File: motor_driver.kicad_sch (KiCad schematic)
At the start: 8 parts, among them J4 Conn_01x06, J5 Conn_01x06, U11 TB6612FNG

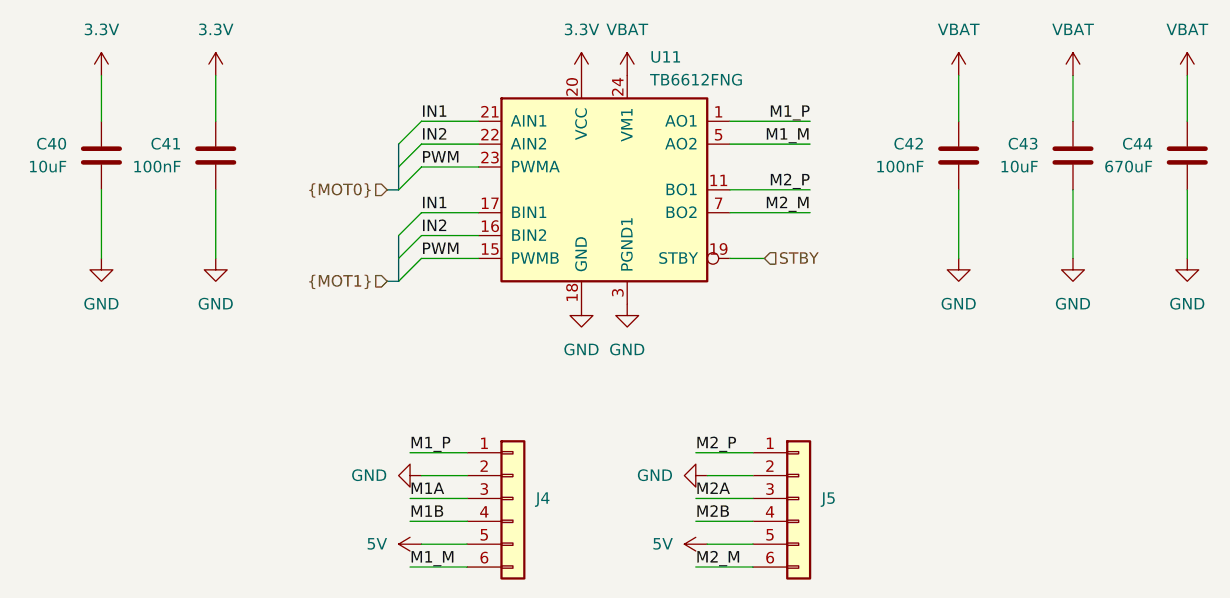
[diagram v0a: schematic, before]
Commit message: Add missing pull-up for CP2102
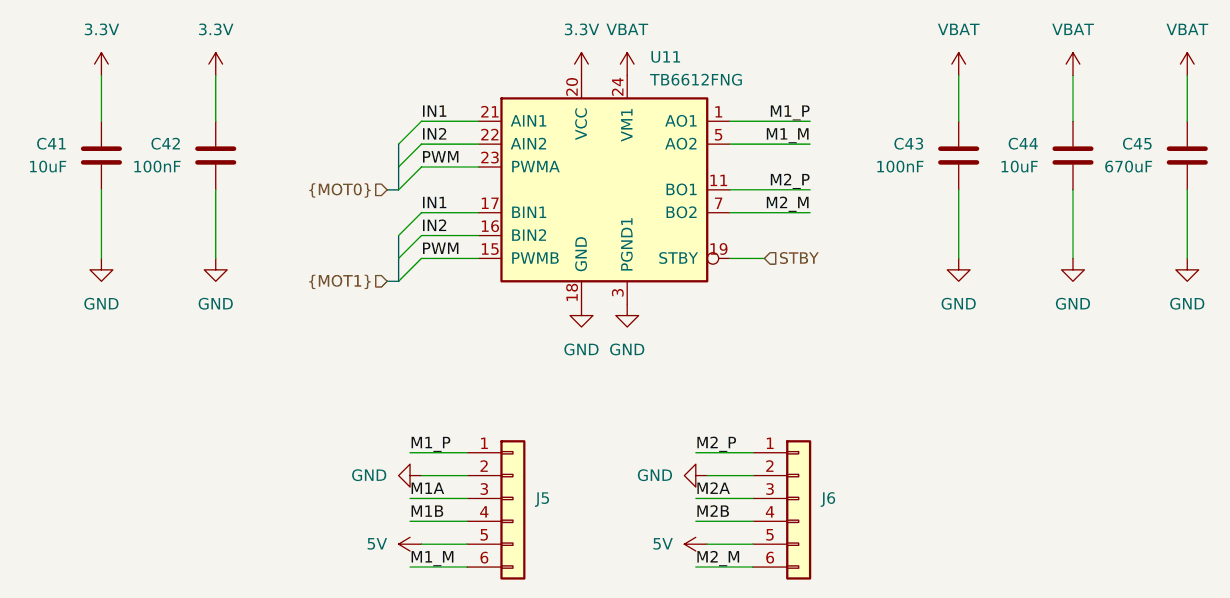
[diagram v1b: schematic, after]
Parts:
- renumbered C40 to C41, C41 to C42, C42 to C43, C43 to C44, C44 to C45, J4 to J5, J5 to J6
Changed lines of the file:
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@@
 		(dnp no)
 		(fields_autoplaced yes)
-		(property "Reference" "#PWR0134"
+		(property "Reference" "#PWR0140"
 			(at 212.09 78.74 0)
 			(effects
@@
 			(project "Tumbler2_Redesign"
 				(path "/f3fd8d79-9d35-4c04-811e-2697a2740958/f393b342-ddad-47d4-8b4e-f21b64e15add"
-					(reference "#PWR0134")
+					(reference "#PWR0140")
 					(unit 1)
 				)
@@
 		(dnp no)
 		(fields_autoplaced yes)
-		(property "Reference" "#PWR0143"
+		(property "Reference" "#PWR0149"
 			(at 152.4 119.38 0)
 			(effects
@@
 			(project "Tumbler2_Redesign"
 				(path "/f3fd8d79-9d35-4c04-811e-2697a2740958/f393b342-ddad-47d4-8b4e-f21b64e15add"
-					(reference "#PWR0143")
+					(reference "#PWR0149")
 					(unit 1)
 				)
@@
 		(dnp no)
 		(fields_autoplaced yes)
-		(property "Reference" "#PWR0129"
+		(property "Reference" "#PWR0137"
 			(at 149.86 78.74 0)
 			(effects
@@
 			(project "Tumbler2_Redesign"
 				(path "/f3fd8d79-9d35-4c04-811e-2697a2740958/f393b342-ddad-47d4-8b4e-f21b64e15add"
-					(reference "#PWR0129")
+					(reference "#PWR0137")
 					(unit 1)
 				)
@@
 		(dnp no)
 		(fields_autoplaced yes)
-		(property "Reference" "#PWR0128"
+		(property "Reference" "#PWR0136"
 			(at 144.78 78.74 0)
 			(effects
@@
 			(project "Tumbler2_Redesign"
 				(path "/f3fd8d79-9d35-4c04-811e-2697a2740958/f393b342-ddad-47d4-8b4e-f21b64e15add"
-					(reference "#PWR0128")
+					(reference "#PWR0136")
 					(unit 1)
 				)
@@
 		(dnp no)
 		(fields_autoplaced yes)
-		(property "Reference" "#PWR0144"
+		(property "Reference" "#PWR0150"
 			(at 130.81 127 0)
 			(effects
@@
 			(project "Tumbler2_Redesign"
 				(path "/f3fd8d79-9d35-4c04-811e-2697a2740958/f393b342-ddad-47d4-8b4e-f21b64e15add"
-					(reference "#PWR0144")
+					(reference "#PWR0150")
 					(unit 1)
 				)
@@
 		(on_board yes)
 		(dnp no)
-		(property "Reference" "C41"
+		(property "Reference" "C42"
 			(at 100.33 82.5499 0)
 			(effects
@@
 			(project "Tumbler2_Redesign"
 				(path "/f3fd8d79-9d35-4c04-811e-2697a2740958/f393b342-ddad-47d4-8b4e-f21b64e15add"
-					(reference "C41")
+					(reference "C42")
 					(unit 1)
 				)
@@
 		(dnp no)
 		(fields_autoplaced yes)
-		(property "Reference" "#PWR0145"
+		(property "Reference" "#PWR0151"
 			(at 162.56 127 0)
 			(effects
@@
 			(project "Tumbler2_Redesign"
 				(path "/f3fd8d79-9d35-4c04-811e-2697a2740958/f393b342-ddad-47d4-8b4e-f21b64e15add"
-					(reference "#PWR0145")
+					(reference "#PWR0151")
 					(unit 1)
 				)
@@
 		(on_board yes)
 		(dnp no)
-		(property "Reference" "C43"
+		(property "Reference" "C44"
 			(at 195.58 82.5499 0)
 			(effects
@@
 			(project "Tumbler2_Redesign"
 				(path "/f3fd8d79-9d35-4c04-811e-2697a2740958/f393b342-ddad-47d4-8b4e-f21b64e15add"
-					(reference "C43")
+					(reference "C44")
 					(unit 1)
 				)
@@
 		(dnp no)
 		(fields_autoplaced yes)
-		(property "Reference" "#PWR0136"
+		(property "Reference" "#PWR0142"
 			(at 104.14 101.6 0)
 			(effects
@@
 			(project "Tumbler2_Redesign"
 				(path "/f3fd8d79-9d35-4c04-811e-2697a2740958/f393b342-ddad-47d4-8b4e-f21b64e15add"
-					(reference "#PWR0136")
+					(reference "#PWR0142")
 					(unit 1)
 				)
@@
 		(dnp no)
 		(fields_autoplaced yes)
-		(property "Reference" "#PWR0137"
+		(property "Reference" "#PWR0146"
 			(at 144.78 106.68 0)
 			(effects
@@
 			(project "Tumbler2_Redesign"
 				(path "/f3fd8d79-9d35-4c04-811e-2697a2740958/f393b342-ddad-47d4-8b4e-f21b64e15add"
-					(reference "#PWR0137")
+					(reference "#PWR0146")
 					(unit 1)
 				)
@@
 		(dnp no)
 		(fields_autoplaced yes)
-		(property "Reference" "#PWR0142"
+		(property "Reference" "#PWR0148"
 			(at 120.65 119.38 0)
 			(effects
@@
 			(project "Tumbler2_Redesign"
 				(path "/f3fd8d79-9d35-4c04-811e-2697a2740958/f393b342-ddad-47d4-8b4e-f21b64e15add"
-					(reference "#PWR0142")
+					(reference "#PWR0148")
 					(unit 1)
 				)
@@
 		(dnp no)
 		(fields_autoplaced yes)
-		(property "Reference" "#PWR0132"
+		(property "Reference" "#PWR0138"
 			(at 186.69 78.74 0)
 			(effects
@@
 			(project "Tumbler2_Redesign"
 				(path "/f3fd8d79-9d35-4c04-811e-2697a2740958/f393b342-ddad-47d4-8b4e-f21b64e15add"
-					(reference "#PWR0132")
+					(reference "#PWR0138")
 					(unit 1)
 				)
@@
 		(dnp no)
 		(fields_autoplaced yes)
-		(property "Reference" "#PWR0141"
+		(property "Reference" "#PWR0145"
 			(at 212.09 101.6 0)
 			(effects
@@
 			(project "Tumbler2_Redesign"
 				(path "/f3fd8d79-9d35-4c04-811e-2697a2740958/f393b342-ddad-47d4-8b4e-f21b64e15add"
-					(reference "#PWR0141")
+					(reference "#PWR0145")
 					(unit 1)
 				)
@@
 		(on_board yes)
 		(dnp no)
-		(property "Reference" "C44"
+		(property "Reference" "C45"
 			(at 208.28 82.5499 0)
 			(effects
@@
 			(project "Tumbler2_Redesign"
 				(path "/f3fd8d79-9d35-4c04-811e-2697a2740958/f393b342-ddad-47d4-8b4e-f21b64e15add"
-					(reference "C44")
+					(reference "C45")
 					(unit 1)
 				)
@@
 		(dnp no)
 		(fields_autoplaced yes)
-		(property "Reference" "#PWR0140"
+		(property "Reference" "#PWR0144"
 			(at 199.39 101.6 0)
 			(effects
@@
 			(project "Tumbler2_Redesign"
 				(path "/f3fd8d79-9d35-4c04-811e-2697a2740958/f393b342-ddad-47d4-8b4e-f21b64e15add"
-					(reference "#PWR0140")
+					(reference "#PWR0144")
 					(unit 1)
 				)
@@
 		(dnp no)
 		(fields_autoplaced yes)
-		(property "Reference" "#PWR0131"
+		(property "Reference" "#PWR0135"
 			(at 104.14 78.74 0)
 			(effects
@@
 			(project "Tumbler2_Redesign"
 				(path "/f3fd8d79-9d35-4c04-811e-2697a2740958/f393b342-ddad-47d4-8b4e-f21b64e15add"
-					(reference "#PWR0131")
+					(reference "#PWR0135")
 					(unit 1)
 				)
@@
 		(on_board yes)
 		(dnp no)
-		(property "Reference" "J5"
+		(property "Reference" "J6"
 			(at 171.45 121.9199 0)
 			(effects
@@
 			(project "Tumbler2_Redesign"
 				(path "/f3fd8d79-9d35-4c04-811e-2697a2740958/f393b342-ddad-47d4-8b4e-f21b64e15add"
-					(reference "J5")
+					(reference "J6")
 					(unit 1)
 				)
@@
 		(dnp no)
 		(fields_autoplaced yes)
-		(property "Reference" "#PWR0139"
+		(property "Reference" "#PWR0143"
 			(at 186.69 101.6 0)
 			(effects
@@
 			(project "Tumbler2_Redesign"
 				(path "/f3fd8d79-9d35-4c04-811e-2697a2740958/f393b342-ddad-47d4-8b4e-f21b64e15add"
-					(reference "#PWR0139")
+					(reference "#PWR0143")
 					(unit 1)
 				)
@@
 		(on_board yes)
 		(dnp no)
-		(property "Reference" "J4"
+		(property "Reference" "J5"
 			(at 139.7 121.9199 0)
 			(effects
@@
 			(project "Tumbler2_Redesign"
 				(path "/f3fd8d79-9d35-4c04-811e-2697a2740958/f393b342-ddad-47d4-8b4e-f21b64e15add"
-					(reference "J4")
+					(reference "J5")
 					(unit 1)
 				)
@@
 		(on_board yes)
 		(dnp no)
-		(property "Reference" "C42"
+		(property "Reference" "C43"
 			(at 182.88 82.5499 0)
 			(effects
@@
 			(project "Tumbler2_Redesign"
 				(path "/f3fd8d79-9d35-4c04-811e-2697a2740958/f393b342-ddad-47d4-8b4e-f21b64e15add"
-					(reference "C42")
+					(reference "C43")
 					(unit 1)
 				)
@@
 		(dnp no)
 		(fields_autoplaced yes)
-		(property "Reference" "#PWR0135"
+		(property "Reference" "#PWR0141"
 			(at 91.44 101.6 0)
 			(effects
@@
 			(project "Tumbler2_Redesign"
 				(path "/f3fd8d79-9d35-4c04-811e-2697a2740958/f393b342-ddad-47d4-8b4e-f21b64e15add"
-					(reference "#PWR0135")
+					(reference "#PWR0141")
 					(unit 1)
 				)
@@
 		(dnp no)
 		(fields_autoplaced yes)
-		(property "Reference" "#PWR0133"
+		(property "Reference" "#PWR0139"
 			(at 199.39 78.74 0)
 			(effects
@@
 			(project "Tumbler2_Redesign"
 				(path "/f3fd8d79-9d35-4c04-811e-2697a2740958/f393b342-ddad-47d4-8b4e-f21b64e15add"
-					(reference "#PWR0133")
+					(reference "#PWR0139")
 					(unit 1)
 				)
@@
 		(dnp no)
 		(fields_autoplaced yes)
-		(property "Reference" "#PWR0138"
+		(property "Reference" "#PWR0147"
 			(at 149.86 106.68 0)
 			(effects
@@
 			(project "Tumbler2_Redesign"
 				(path "/f3fd8d79-9d35-4c04-811e-2697a2740958/f393b342-ddad-47d4-8b4e-f21b64e15add"
-					(reference "#PWR0138")
+					(reference "#PWR0147")
 					(unit 1)
 				)
@@
 		(dnp no)
 		(fields_autoplaced yes)
-		(property "Reference" "#PWR0130"
+		(property "Reference" "#PWR0134"
 			(at 91.44 78.74 0)
 			(effects
@@
 			(project "Tumbler2_Redesign"
 				(path "/f3fd8d79-9d35-4c04-811e-2697a2740958/f393b342-ddad-47d4-8b4e-f21b64e15add"
-					(reference "#PWR0130")
+					(reference "#PWR0134")
 					(unit 1)
 				)
@@
 		(on_board yes)
 		(dnp no)
-		(property "Reference" "C40"
+		(property "Reference" "C41"
 			(at 87.63 82.5499 0)
 			(effects
@@
 			(project "Tumbler2_Redesign"
 				(path "/f3fd8d79-9d35-4c04-811e-2697a2740958/f393b342-ddad-47d4-8b4e-f21b64e15add"
-					(reference "C40")
-					(unit 1)
-				)
+					(reference "C41")
+					(unit 1)
+				)

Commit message: Remove caps for BTN and GPIO0
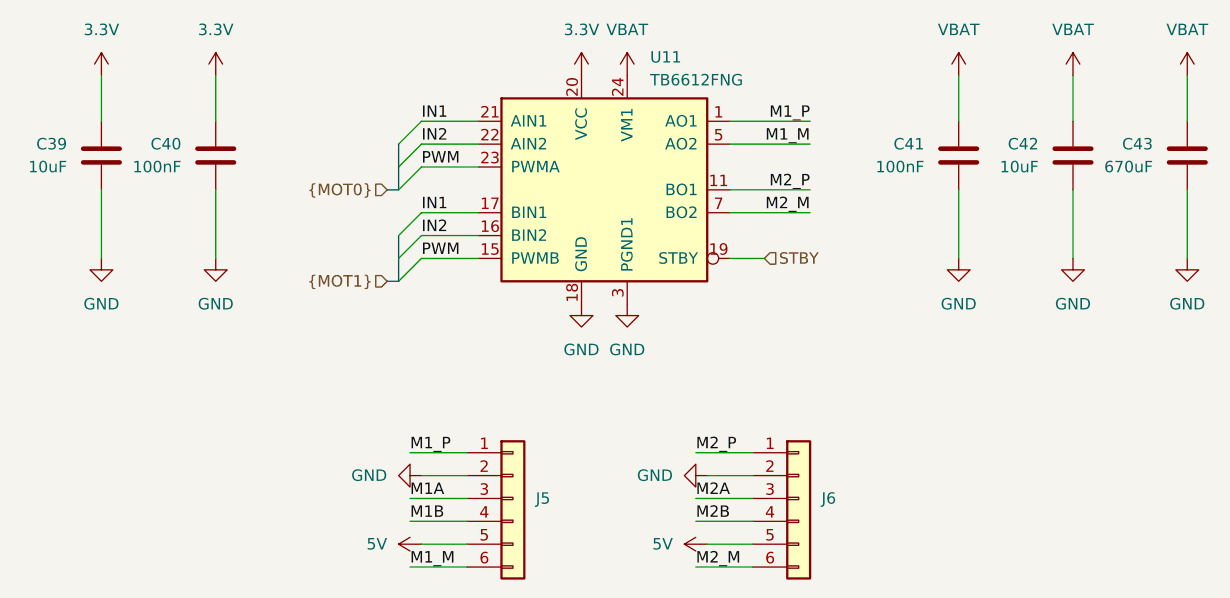
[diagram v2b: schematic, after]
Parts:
- renumbered C41 to C39, C42 to C40, C43 to C41, C44 to C42, C45 to C43
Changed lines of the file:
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@@
 		(dnp no)
 		(fields_autoplaced yes)
-		(property "Reference" "#PWR0140"
+		(property "Reference" "#PWR0138"
 			(at 212.09 78.74 0)
 			(effects
@@
 			(project "Tumbler2_Redesign"
 				(path "/f3fd8d79-9d35-4c04-811e-2697a2740958/f393b342-ddad-47d4-8b4e-f21b64e15add"
-					(reference "#PWR0140")
+					(reference "#PWR0138")
 					(unit 1)
 				)
@@
 		(dnp no)
 		(fields_autoplaced yes)
-		(property "Reference" "#PWR0149"
+		(property "Reference" "#PWR0147"
 			(at 152.4 119.38 0)
 			(effects
@@
 			(project "Tumbler2_Redesign"
 				(path "/f3fd8d79-9d35-4c04-811e-2697a2740958/f393b342-ddad-47d4-8b4e-f21b64e15add"
-					(reference "#PWR0149")
+					(reference "#PWR0147")
 					(unit 1)
 				)
@@
 		(dnp no)
 		(fields_autoplaced yes)
-		(property "Reference" "#PWR0137"
+		(property "Reference" "#PWR0135"
 			(at 149.86 78.74 0)
 			(effects
@@
 			(project "Tumbler2_Redesign"
 				(path "/f3fd8d79-9d35-4c04-811e-2697a2740958/f393b342-ddad-47d4-8b4e-f21b64e15add"
-					(reference "#PWR0137")
+					(reference "#PWR0135")
 					(unit 1)
 				)
@@
 		(dnp no)
 		(fields_autoplaced yes)
-		(property "Reference" "#PWR0136"
+		(property "Reference" "#PWR0134"
 			(at 144.78 78.74 0)
 			(effects
@@
 			(project "Tumbler2_Redesign"
 				(path "/f3fd8d79-9d35-4c04-811e-2697a2740958/f393b342-ddad-47d4-8b4e-f21b64e15add"
-					(reference "#PWR0136")
+					(reference "#PWR0134")
 					(unit 1)
 				)
@@
 		(dnp no)
 		(fields_autoplaced yes)
-		(property "Reference" "#PWR0150"
+		(property "Reference" "#PWR0148"
 			(at 130.81 127 0)
 			(effects
@@
 			(project "Tumbler2_Redesign"
 				(path "/f3fd8d79-9d35-4c04-811e-2697a2740958/f393b342-ddad-47d4-8b4e-f21b64e15add"
-					(reference "#PWR0150")
+					(reference "#PWR0148")
 					(unit 1)
 				)
@@
 		(on_board yes)
 		(dnp no)
-		(property "Reference" "C42"
+		(property "Reference" "C40"
 			(at 100.33 82.5499 0)
 			(effects
@@
 			(project "Tumbler2_Redesign"
 				(path "/f3fd8d79-9d35-4c04-811e-2697a2740958/f393b342-ddad-47d4-8b4e-f21b64e15add"
-					(reference "C42")
+					(reference "C40")
 					(unit 1)
 				)
@@
 		(dnp no)
 		(fields_autoplaced yes)
-		(property "Reference" "#PWR0151"
+		(property "Reference" "#PWR0149"
 			(at 162.56 127 0)
 			(effects
@@
 			(project "Tumbler2_Redesign"
 				(path "/f3fd8d79-9d35-4c04-811e-2697a2740958/f393b342-ddad-47d4-8b4e-f21b64e15add"
-					(reference "#PWR0151")
+					(reference "#PWR0149")
 					(unit 1)
 				)
@@
 		(on_board yes)
 		(dnp no)
-		(property "Reference" "C44"
+		(property "Reference" "C42"
 			(at 195.58 82.5499 0)
 			(effects
@@
 			(project "Tumbler2_Redesign"
 				(path "/f3fd8d79-9d35-4c04-811e-2697a2740958/f393b342-ddad-47d4-8b4e-f21b64e15add"
-					(reference "C44")
+					(reference "C42")
 					(unit 1)
 				)
@@
 		(dnp no)
 		(fields_autoplaced yes)
-		(property "Reference" "#PWR0142"
+		(property "Reference" "#PWR0140"
 			(at 104.14 101.6 0)
 			(effects
@@
 			(project "Tumbler2_Redesign"
 				(path "/f3fd8d79-9d35-4c04-811e-2697a2740958/f393b342-ddad-47d4-8b4e-f21b64e15add"
-					(reference "#PWR0142")
+					(reference "#PWR0140")
 					(unit 1)
 				)
@@
 		(dnp no)
 		(fields_autoplaced yes)
-		(property "Reference" "#PWR0146"
+		(property "Reference" "#PWR0144"
 			(at 144.78 106.68 0)
 			(effects
@@
 			(project "Tumbler2_Redesign"
 				(path "/f3fd8d79-9d35-4c04-811e-2697a2740958/f393b342-ddad-47d4-8b4e-f21b64e15add"
-					(reference "#PWR0146")
+					(reference "#PWR0144")
 					(unit 1)
 				)
@@
 		(dnp no)
 		(fields_autoplaced yes)
-		(property "Reference" "#PWR0148"
+		(property "Reference" "#PWR0146"
 			(at 120.65 119.38 0)
 			(effects
@@
 			(project "Tumbler2_Redesign"
 				(path "/f3fd8d79-9d35-4c04-811e-2697a2740958/f393b342-ddad-47d4-8b4e-f21b64e15add"
-					(reference "#PWR0148")
+					(reference "#PWR0146")
 					(unit 1)
 				)
@@
 		(dnp no)
 		(fields_autoplaced yes)
-		(property "Reference" "#PWR0138"
+		(property "Reference" "#PWR0136"
 			(at 186.69 78.74 0)
 			(effects
@@
 			(project "Tumbler2_Redesign"
 				(path "/f3fd8d79-9d35-4c04-811e-2697a2740958/f393b342-ddad-47d4-8b4e-f21b64e15add"
-					(reference "#PWR0138")
+					(reference "#PWR0136")
 					(unit 1)
 				)
@@
 		(dnp no)
 		(fields_autoplaced yes)
-		(property "Reference" "#PWR0145"
+		(property "Reference" "#PWR0143"
 			(at 212.09 101.6 0)
 			(effects
@@
 			(project "Tumbler2_Redesign"
 				(path "/f3fd8d79-9d35-4c04-811e-2697a2740958/f393b342-ddad-47d4-8b4e-f21b64e15add"
-					(reference "#PWR0145")
+					(reference "#PWR0143")
 					(unit 1)
 				)
@@
 		(on_board yes)
 		(dnp no)
-		(property "Reference" "C45"
+		(property "Reference" "C43"
 			(at 208.28 82.5499 0)
 			(effects
@@
 			(project "Tumbler2_Redesign"
 				(path "/f3fd8d79-9d35-4c04-811e-2697a2740958/f393b342-ddad-47d4-8b4e-f21b64e15add"
-					(reference "C45")
+					(reference "C43")
 					(unit 1)
 				)
@@
 		(dnp no)
 		(fields_autoplaced yes)
-		(property "Reference" "#PWR0144"
+		(property "Reference" "#PWR0142"
 			(at 199.39 101.6 0)
 			(effects
@@
 			(project "Tumbler2_Redesign"
 				(path "/f3fd8d79-9d35-4c04-811e-2697a2740958/f393b342-ddad-47d4-8b4e-f21b64e15add"
-					(reference "#PWR0144")
+					(reference "#PWR0142")
 					(unit 1)
 				)
@@
 		(dnp no)
 		(fields_autoplaced yes)
-		(property "Reference" "#PWR0135"
+		(property "Reference" "#PWR0133"
 			(at 104.14 78.74 0)
 			(effects
@@
 			(project "Tumbler2_Redesign"
 				(path "/f3fd8d79-9d35-4c04-811e-2697a2740958/f393b342-ddad-47d4-8b4e-f21b64e15add"
-					(reference "#PWR0135")
+					(reference "#PWR0133")
 					(unit 1)
 				)
@@
 		(dnp no)
 		(fields_autoplaced yes)
-		(property "Reference" "#PWR0143"
+		(property "Reference" "#PWR0141"
 			(at 186.69 101.6 0)
 			(effects
@@
 			(project "Tumbler2_Redesign"
 				(path "/f3fd8d79-9d35-4c04-811e-2697a2740958/f393b342-ddad-47d4-8b4e-f21b64e15add"
-					(reference "#PWR0143")
+					(reference "#PWR0141")
 					(unit 1)
 				)
@@
 		(on_board yes)
 		(dnp no)
-		(property "Reference" "C43"
+		(property "Reference" "C41"
 			(at 182.88 82.5499 0)
 			(effects
@@
 			(project "Tumbler2_Redesign"
 				(path "/f3fd8d79-9d35-4c04-811e-2697a2740958/f393b342-ddad-47d4-8b4e-f21b64e15add"
-					(reference "C43")
+					(reference "C41")
 					(unit 1)
 				)
@@
 		(dnp no)
 		(fields_autoplaced yes)
-		(property "Reference" "#PWR0141"
+		(property "Reference" "#PWR0139"
 			(at 91.44 101.6 0)
 			(effects
@@
 			(project "Tumbler2_Redesign"
 				(path "/f3fd8d79-9d35-4c04-811e-2697a2740958/f393b342-ddad-47d4-8b4e-f21b64e15add"
-					(reference "#PWR0141")
+					(reference "#PWR0139")
 					(unit 1)
 				)
@@
 		(dnp no)
 		(fields_autoplaced yes)
-		(property "Reference" "#PWR0139"
+		(property "Reference" "#PWR0137"
 			(at 199.39 78.74 0)
 			(effects
@@
 			(project "Tumbler2_Redesign"
 				(path "/f3fd8d79-9d35-4c04-811e-2697a2740958/f393b342-ddad-47d4-8b4e-f21b64e15add"
-					(reference "#PWR0139")
+					(reference "#PWR0137")
 					(unit 1)
 				)
@@
 		(dnp no)
 		(fields_autoplaced yes)
-		(property "Reference" "#PWR0147"
+		(property "Reference" "#PWR0145"
 			(at 149.86 106.68 0)
 			(effects
@@
 			(project "Tumbler2_Redesign"
 				(path "/f3fd8d79-9d35-4c04-811e-2697a2740958/f393b342-ddad-47d4-8b4e-f21b64e15add"
-					(reference "#PWR0147")
+					(reference "#PWR0145")
 					(unit 1)
 				)
@@
 		(dnp no)
 		(fields_autoplaced yes)
-		(property "Reference" "#PWR0134"
+		(property "Reference" "#PWR0132"
 			(at 91.44 78.74 0)
 			(effects
@@
 			(project "Tumbler2_Redesign"
 				(path "/f3fd8d79-9d35-4c04-811e-2697a2740958/f393b342-ddad-47d4-8b4e-f21b64e15add"
-					(reference "#PWR0134")
+					(reference "#PWR0132")
 					(unit 1)
 				)
@@
 		(on_board yes)
 		(dnp no)
-		(property "Reference" "C41"
+		(property "Reference" "C39"
 			(at 87.63 82.5499 0)
 			(effects
@@
 			(project "Tumbler2_Redesign"
 				(path "/f3fd8d79-9d35-4c04-811e-2697a2740958/f393b342-ddad-47d4-8b4e-f21b64e15add"
-					(reference "C41")
-					(unit 1)
-				)
+					(reference "C39")
+					(unit 1)
+				)
